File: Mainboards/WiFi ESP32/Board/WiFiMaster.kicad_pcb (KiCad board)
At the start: 2 copper layers, 67.4 x 54.3 mm, 49 parts, among them IC1 MCP170X, IC2 NCP1117ST, J1 Barrel_Jack_Switch, J2 Conn_02x04_Odd_Even, U2 SN74LVC8T245, U3 SN74LVC8T245, U4 TPS56220, U5 ESP32-WROOM-32U, X1 AKL18X-04W, X2 ALLSERIALMASTERM

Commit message: Added new boards
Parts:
- S1: footprint WiFiMaster:B3F-31XX -> Button_Switch_THT:SW_Tactile_SPST_Angled_PTS645Vx58-2LFS
- moved S1 2.58 mm to (162.8, 128.5), turned to 180 degrees
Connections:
- S1 pad 1: GND -> /BTN
- S1 pad 2: /BTN -> GND

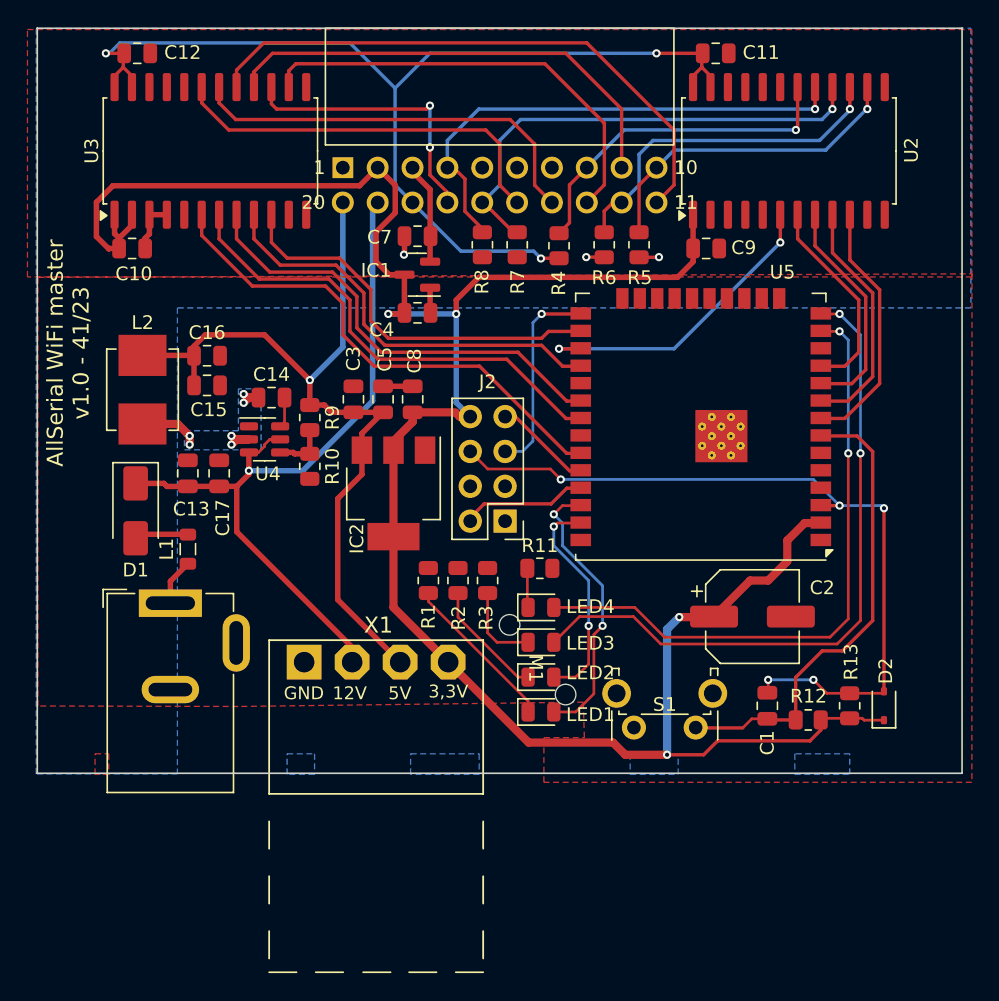
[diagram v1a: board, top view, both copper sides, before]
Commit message: Update TTY CL slave board
Add ESP32 S3 WiFi MasterBoard
Update libs
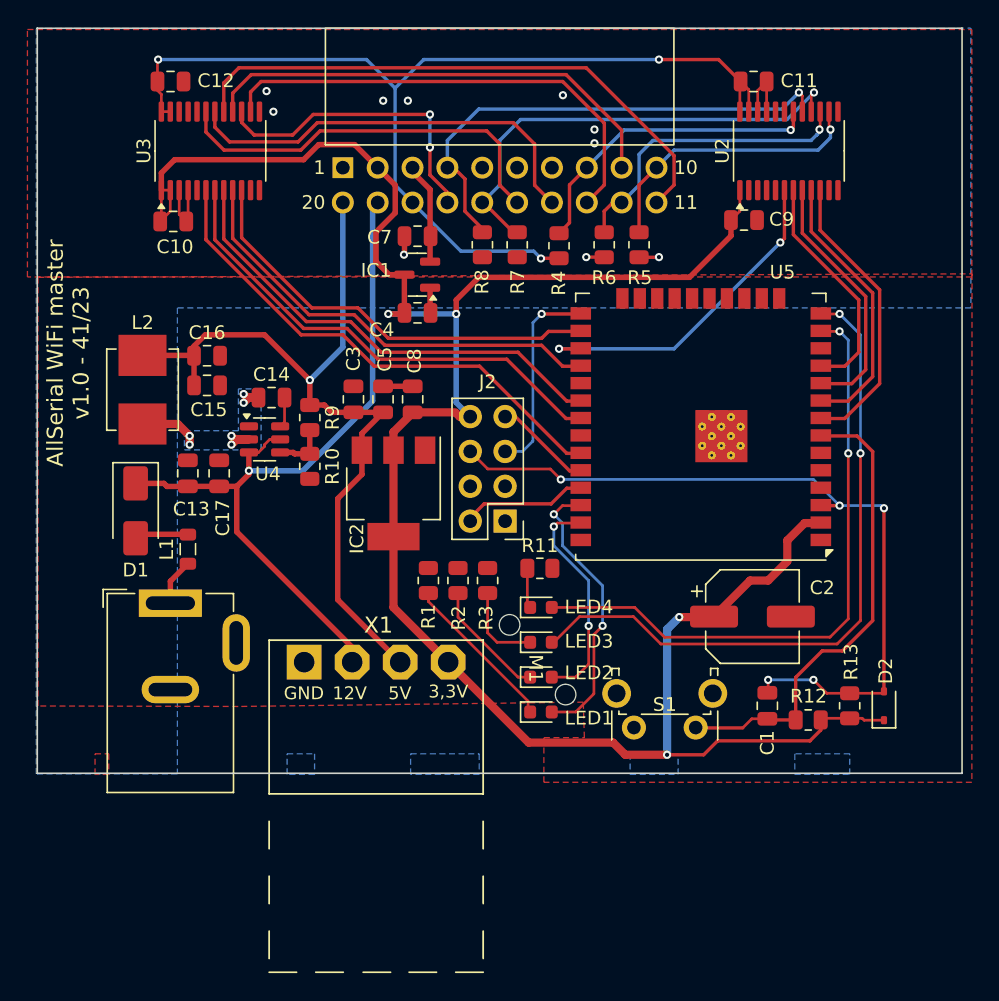
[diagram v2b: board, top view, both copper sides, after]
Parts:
- LED1: value LED3MM -> red; footprint LED_SMD:LED_0805_2012Metric -> LED_SMD:LED_0603_1608Metric
- LED2: value LED3MM -> green; footprint LED_SMD:LED_0805_2012Metric -> LED_SMD:LED_0603_1608Metric
- LED3: value LED3MM -> yellow; footprint LED_SMD:LED_0805_2012Metric -> LED_SMD:LED_0603_1608Metric
- LED4: value LED3MM -> blue; footprint LED_SMD:LED_0805_2012Metric -> LED_SMD:LED_0603_1608Metric
- R11: value 120 -> 22
- U2, U3: footprint Package_SO:SOIC-24W_7.5x15.4mm_P1.27mm -> Package_SO:TSSOP-24_4.4x7.8mm_P0.65mm
- moved C10 3.59 mm to (124.7, 91.7)
- moved C9 3.45 mm to (166.3, 91.6)
- moved C11 3.44 mm to (167.0, 81.5)
- moved C12 3.18 mm to (124.5, 81.5)
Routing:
- net GND: track 12.0 -> 17.6 mm, vias 3 -> 10
- net /RI_B: track 24.0 -> 20.8 mm
- net /DSR_B: track 25.5 -> 22.4 mm
- net +3.3V: track 166.3 -> 163.3 mm
- net /RI_A: track 18.6 -> 21.3 mm
- net /DTR_B: track 32.5 -> 35.1 mm
- net /DSR_A: track 17.6 -> 20.0 mm
- net /DTR_A: track 29.0 -> 31.4 mm
- net VBUS: track 77.7 -> 75.3 mm
- net /DCD_A: track 16.5 -> 18.7 mm
- net /RXD_B: track 25.2 -> 23.0 mm
- net /TXD_A: track 30.7 -> 32.7 mm
- net /CTS_A: track 15.1 -> 17.0 mm
- net /RXD_A: track 22.9 -> 24.8 mm
- net /TXD_B: track 20.2 -> 22.0 mm
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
